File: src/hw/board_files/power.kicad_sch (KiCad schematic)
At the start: 38 parts, among them J1 Conn_01x03_Pin, J6 Screw_Terminal_01x03, P1 USB_C_Plug_USB2.0, SW1 SW_PWR, U1 FT234XD-R, U2 MCP73871, U3 TPS63031DSKR

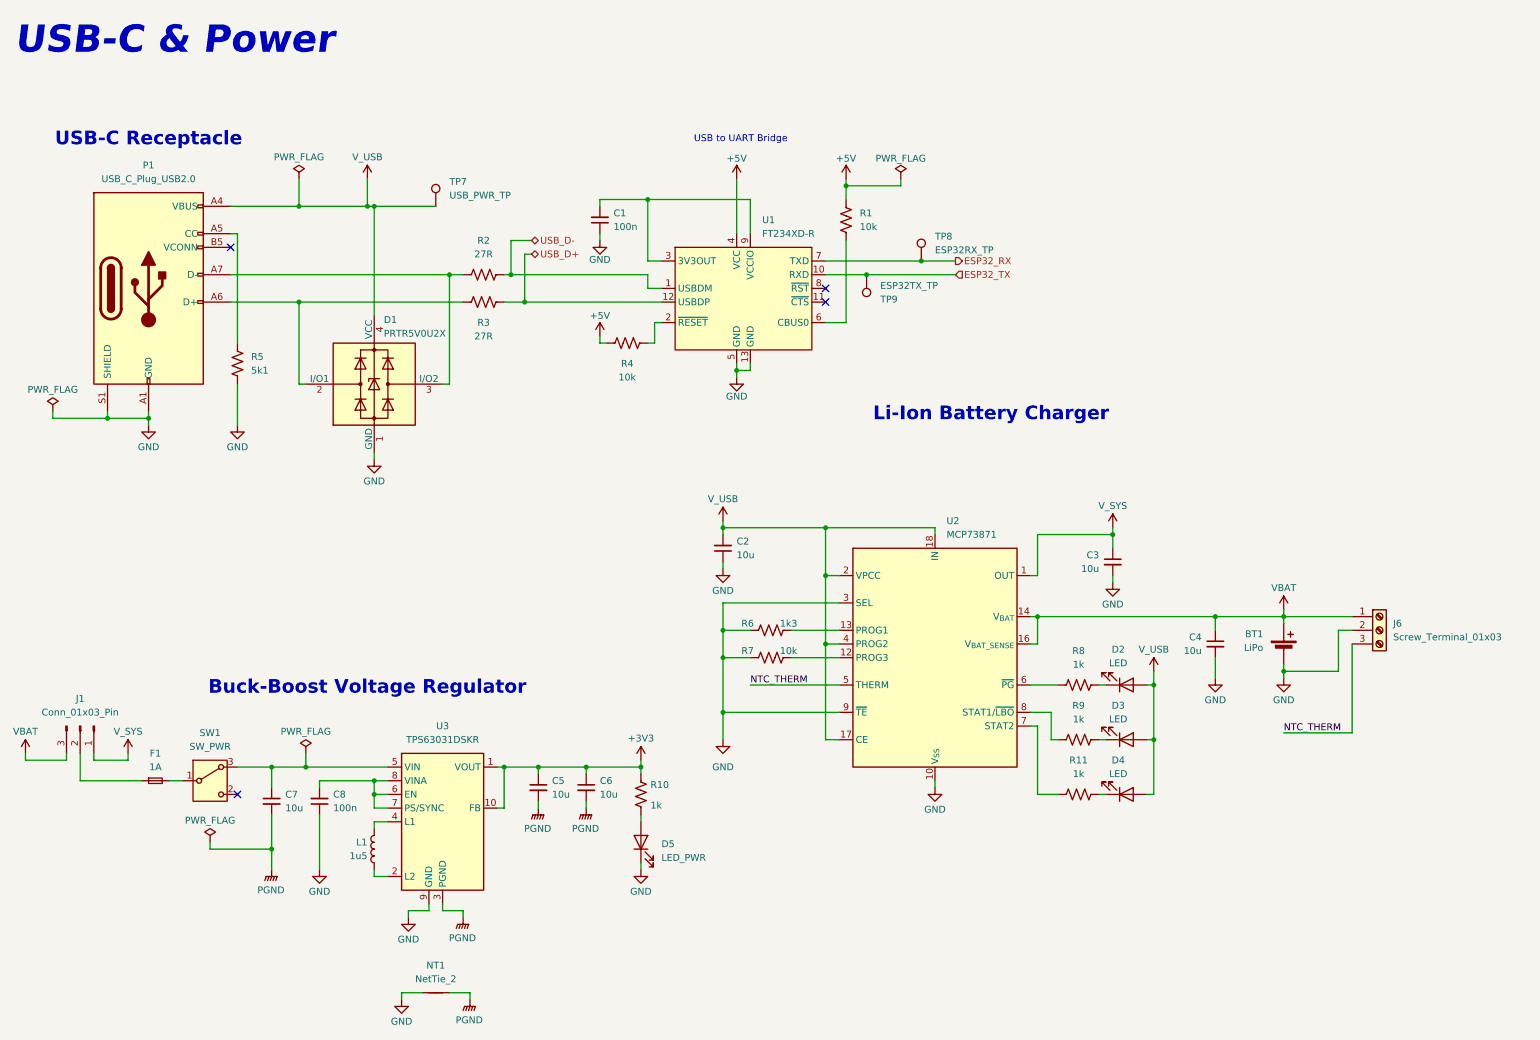
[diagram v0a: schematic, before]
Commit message: Lots of layout progress, changed some references (need to update BOM)
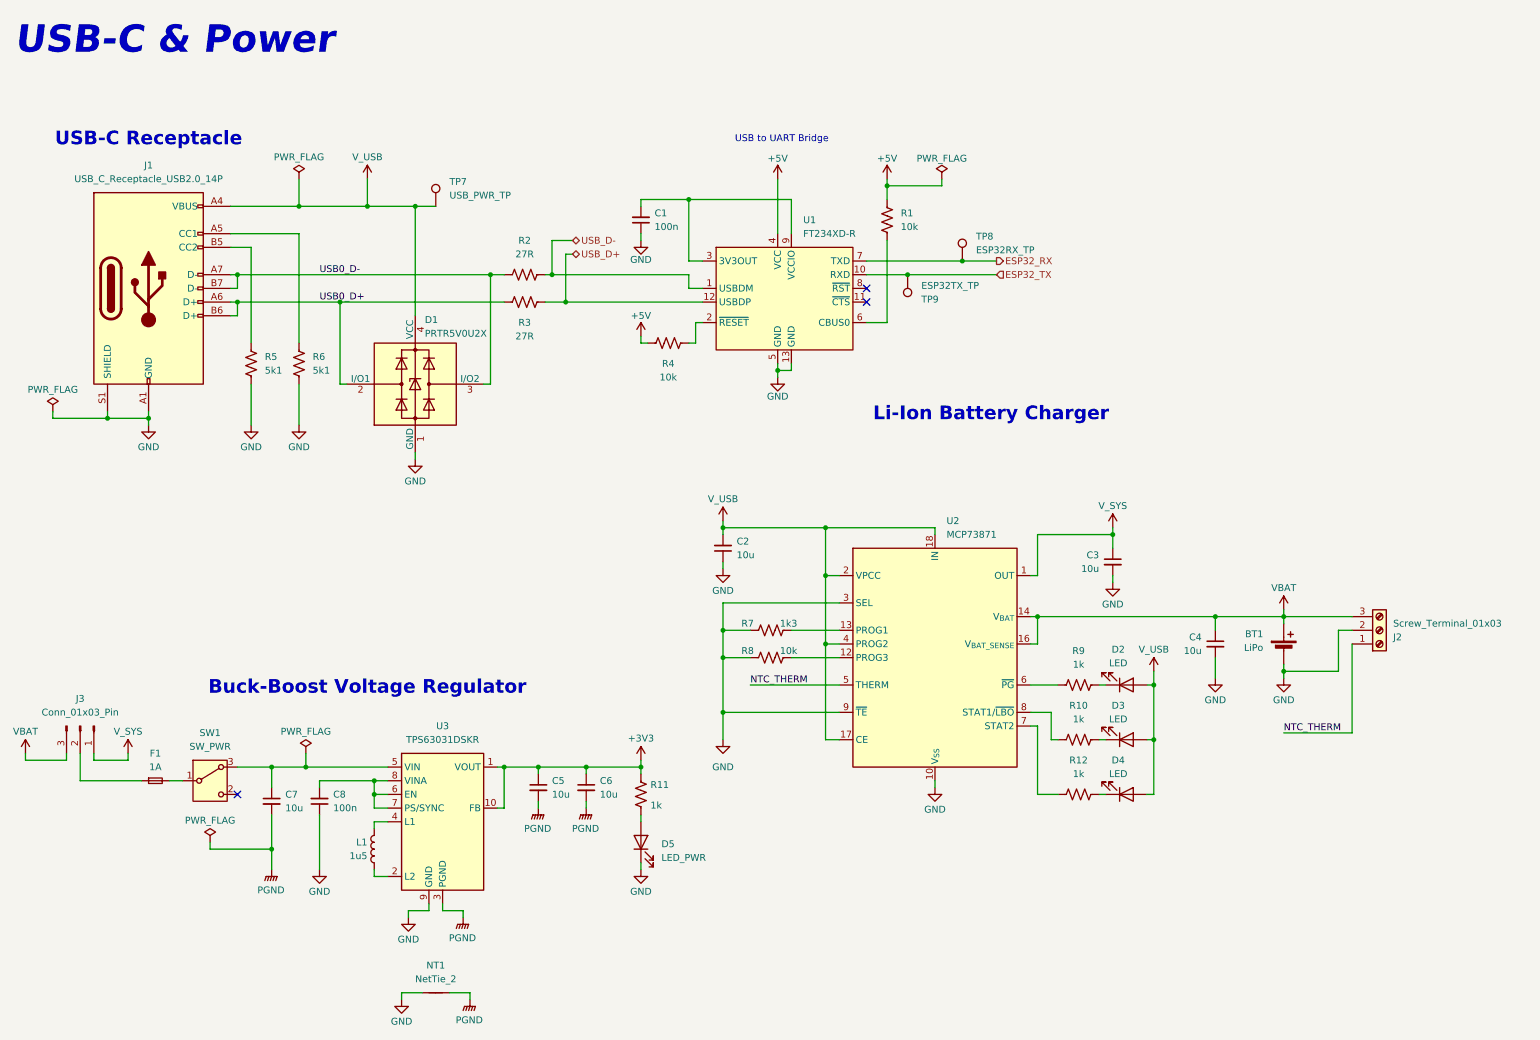
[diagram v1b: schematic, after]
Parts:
- removed P1: USB_C_Plug_USB2.0, Connector_USB:USB_C_Receptacle_GCT_USB4110, symbol Connector:USB_C_Plug_USB2.0
- added J1: USB_C_Receptacle_USB2.0_14P, Connector_USB:USB_C_Receptacle_GCT_USB4105-xx-A_16P_TopMnt_Horizontal, symbol Connector:USB_C_Receptacle_USB2.0_14P
- added R5: 5k1, Resistor_SMD:R_0603_1608Metric_Pad0.98x0.95mm_HandSolder, symbol Device:R_US
- renumbered J6 to J2, J1 to J3, R9 to R10, R10 to R11, R11 to R12, R5 to R6, R6 to R7, R7 to R8, R8 to R9
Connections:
- net GND: now also J1.A1 (GND), J1.A12 (GND), J1.B1 (GND), J1.B12 (GND), J1.S1 (SHIELD), R5.1
- net NTC_THERM: now also J2.1 (Pin_1); no longer J2.3 (Pin_3)
- net VBAT: now also J2.3 (Pin_3); no longer J2.1 (Pin_1)
- net V_USB: now also J1.A4 (VBUS), J1.A9 (VBUS), J1.B4 (VBUS), J1.B9 (VBUS)
- net USB0_D-: now reaches D1.3 (I/O2), R2.2
- net USB0_D-: now also J1.A7 (D-), J1.B7 (D-)
- net USB0_D+: now reaches D1.2 (I/O1), R3.2
- net USB0_D+: now also J1.A6 (D+), J1.B6 (D+)
- net at R6.2: now also J1.A5 (CC1)
- new net: J1.B5 (CC2), R5.2
- no-connect marks 4 -> 3
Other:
- moved on the sheet: C1, D1, R1, R2, R3, R4, R6, TP8, TP9, U1

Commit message: Layout updates
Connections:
- net +5V is gone; now on net +3V3: R1.1, R4.2, U1.4 (VCC)
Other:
- moved on the sheet: BT1, C2, C3, C4, C5, C6, C7, C8, D2, D3, D4, D5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

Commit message: Minor schematic updates
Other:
- note added: "LiPo Battery"
- note added: "LiPo Battery Charger"
- note removed: "Li-Ion Battery Charger"
- moved on the sheet: BT1, J2
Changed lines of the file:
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@@
 	(text "USB-C Receptacle"
 		(exclude_from_sim no)
-		(at 39.37 37.084 0)
+		(at 40.386 34.036 0)
 		(effects
 			(font
@@
 		)
 	)
-	(text "Li-Ion Battery Charger"
+	(text "LiPo Battery Charger"
 		(exclude_from_sim no)
 		(at 204.724 102.362 0)
@@
 	(text "USB to UART Bridge"
 		(exclude_from_sim no)
-		(at 156.972 37.084 0)
+		(at 155.702 34.036 0)
 		(effects
 			(font
-				(size 1.27 1.27)
+				(size 2.54 2.54)
+				(thickness 0.508)
+				(bold yes)
+			)
+		)
+	)
+	(text "LiPo Battery"
+		(exclude_from_sim no)
+		(at 240.284 34.544 0)
+		(effects
+			(font
+				(size 2.54 2.54)
+				(thickness 0.508)
+				(bold yes)
 			)
 		)
@@
 	)
 	(junction
-		(at 219.71 35.56)
+		(at 224.79 62.23)
 		(diameter 0)
 		(color 0 0 0 0)
@@
 	)
 	(junction
-		(at 219.71 25.4)
+		(at 224.79 52.07)
 		(diameter 0)
 		(color 0 0 0 0)
@@
 	(wire
 		(pts
-			(xy 219.71 34.29) (xy 219.71 35.56)
+			(xy 224.79 60.96) (xy 224.79 62.23)
 		)
 		(stroke
@@
 	(wire
 		(pts
-			(xy 219.71 25.4) (xy 219.71 26.67)
+			(xy 224.79 52.07) (xy 224.79 53.34)
 		)
 		(stroke
@@
 	(wire
 		(pts
-			(xy 232.41 30.48) (xy 232.41 46.99)
+			(xy 237.49 57.15) (xy 237.49 73.66)
 		)
 		(stroke
@@
 	(wire
 		(pts
-			(xy 232.41 27.94) (xy 229.87 27.94)
+			(xy 237.49 54.61) (xy 234.95 54.61)
 		)
 		(stroke
@@
 	(wire
 		(pts
-			(xy 219.71 46.99) (xy 232.41 46.99)
+			(xy 224.79 73.66) (xy 237.49 73.66)
 		)
 		(stroke
@@
 	(wire
 		(pts
-			(xy 219.71 35.56) (xy 219.71 36.83)
+			(xy 224.79 62.23) (xy 224.79 63.5)
 		)
 		(stroke
@@
 	(wire
 		(pts
-			(xy 229.87 27.94) (xy 229.87 35.56)
+			(xy 234.95 54.61) (xy 234.95 62.23)
 		)
 		(stroke
@@
 	(wire
 		(pts
-			(xy 219.71 24.13) (xy 219.71 25.4)
+			(xy 224.79 50.8) (xy 224.79 52.07)
 		)
 		(stroke
@@
 	(wire
 		(pts
-			(xy 229.87 35.56) (xy 219.71 35.56)
+			(xy 234.95 62.23) (xy 224.79 62.23)
 		)
 		(stroke
@@
 	(wire
 		(pts
-			(xy 219.71 25.4) (xy 232.41 25.4)
+			(xy 224.79 52.07) (xy 237.49 52.07)
 		)
 		(stroke
@@
 	)
 	(label "NTC_THERM"
-		(at 219.71 46.99 0)
+		(at 224.79 73.66 0)
 		(effects
 			(font
@@
 	(symbol
 		(lib_id "power:GND")
-		(at 219.71 36.83 0)
+		(at 224.79 63.5 0)
 		(unit 1)
 		(exclude_from_sim no)
@@
 		(dnp no)
 		(property "Reference" "#PWR018"
-			(at 219.71 43.18 0)
+			(at 224.79 69.85 0)
 			(effects
 				(font
@@
 		)
 		(property "Value" "GND"
-			(at 219.71 40.894 0)
+			(at 224.79 67.564 0)
 			(effects
 				(font
@@
 		)
 		(property "Footprint" ""
-			(at 219.71 36.83 0)
+			(at 224.79 63.5 0)
 			(effects
 				(font
@@
 		)
 		(property "Datasheet" ""
-			(at 219.71 36.83 0)
+			(at 224.79 63.5 0)
 			(effects
 				(font
@@
 		)
 		(property "Description" "Power symbol creates a global label with name \"GND\" , ground"
-			(at 219.71 36.83 0)
+			(at 224.79 63.5 0)
 			(effects
 				(font
@@
 	(symbol
 		(lib_id "Connector:Screw_Terminal_01x03")
-		(at 237.49 27.94 0)
+		(at 242.57 54.61 0)
 		(mirror x)
 		(unit 1)
@@
 		(dnp no)
 		(property "Reference" "J2"
-			(at 240.03 29.2101 0)
+			(at 245.11 55.8801 0)
 			(effects
 				(font
@@
 		)
 		(property "Value" "Screw_Terminal_01x03"
-			(at 240.03 26.6701 0)
+			(at 245.11 53.3401 0)
 			(effects
 				(font
@@
 		)
 		(property "Footprint" "TerminalBlock_Phoenix:TerminalBlock_Phoenix_MPT-0,5-3-2.54_1x03_P2.54mm_Horizontal"
-			(at 237.49 27.94 0)
+			(at 242.57 54.61 0)
 			(effects
 				(font
@@
 		)
 		(property "Datasheet" "~"
-			(at 237.49 27.94 0)
+			(at 242.57 54.61 0)
 			(effects
 				(font
@@
 		)
 		(property "Description" "Generic screw terminal, single row, 01x03, script generated (kicad-library-utils/schlib/autogen/connector/)"
-			(at 237.49 27.94 0)
+			(at 242.57 54.61 0)
 			(effects
 				(font
@@
 	(symbol
 		(lib_id "power:+3V3")
-		(at 219.71 24.13 0)
+		(at 224.79 50.8 0)
 		(unit 1)
 		(exclude_from_sim no)
@@
 		(dnp no)
 		(property "Reference" "#PWR081"
-			(at 219.71 27.94 0)
+			(at 224.79 54.61 0)
 			(effects
 				(font
@@
 		)
 		(property "Value" "VBAT"
-			(at 219.71 20.066 0)
+			(at 224.79 46.736 0)
 			(effects
 				(font
@@
 		)
 		(property "Footprint" ""
-			(at 219.71 24.13 0)
+			(at 224.79 50.8 0)
 			(effects
 				(font
@@
 		)
 		(property "Datasheet" ""
-			(at 219.71 24.13 0)
+			(at 224.79 50.8 0)
 			(effects
 				(font
@@
 		)
 		(property "Description" "Power symbol creates a global label with name \"+3V3\""
-			(at 219.71 24.13 0)
+			(at 224.79 50.8 0)
 			(effects
 				(font
@@
 	(symbol
 		(lib_id "Device:Battery_Cell")
-		(at 219.71 31.75 0)
+		(at 224.79 58.42 0)
 		(unit 1)
 		(exclude_from_sim no)
@@
 		(fields_autoplaced yes)
 		(property "Reference" "BT1"
-			(at 215.9 28.6384 0)
+			(at 220.98 55.3084 0)
 			(effects
 				(font
@@
 		)
 		(property "Value" "LiPo"
-			(at 215.9 31.1784 0)
+			(at 220.98 57.8484 0)
 			(effects
 				(font
@@
 		)
 		(property "Footprint" "Connector_JST:JST_PH_S2B-PH-K_1x02_P2.00mm_Horizontal"
-			(at 219.71 30.226 90)
+			(at 224.79 56.896 90)
 			(effects
 				(font
@@
 		)
 		(property "Datasheet" "https://www.adafruit.com/product/328"
-			(at 219.71 30.226 90)
+			(at 224.79 56.896 90)
 			(effects
 				(font
@@
 		)
 		(property "Description" "Single-cell battery"
-			(at 219.71 31.75 0)
+			(at 224.79 58.42 0)
 			(effects
 				(font

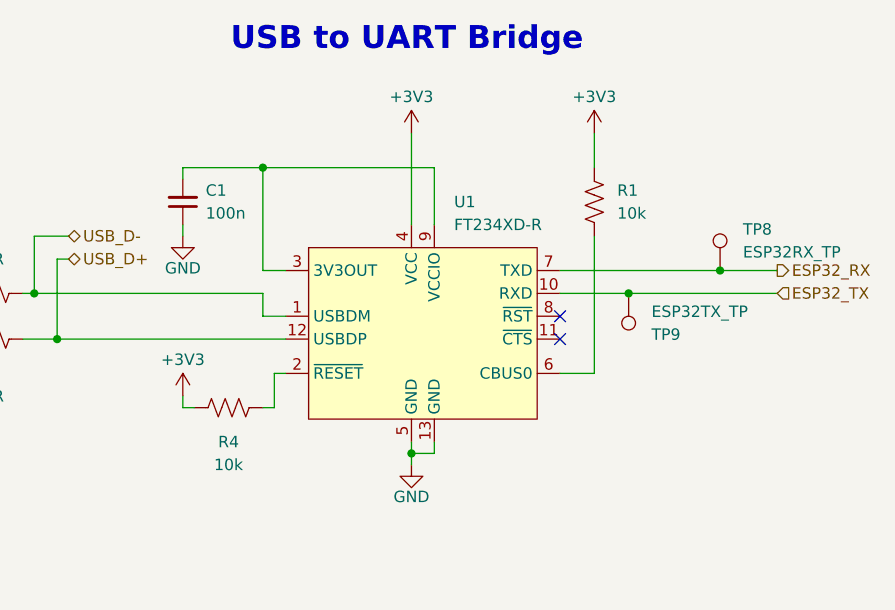
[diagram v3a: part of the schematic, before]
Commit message: Changed fuel gauge IC. Need to update component references and BOM.
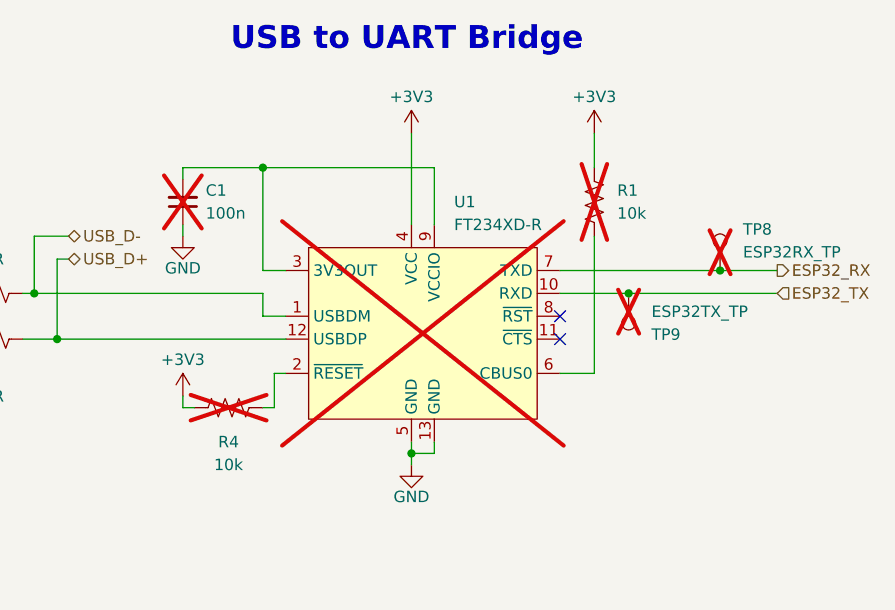
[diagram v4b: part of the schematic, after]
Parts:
- C1, R1, R4, TP8, TP9, U1: now not fitted
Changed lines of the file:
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@@
 		(exclude_from_sim no)
 		(in_bom yes)
-		(on_board yes)
-		(dnp no)
+		(on_board no)
+		(dnp yes)
 		(fields_autoplaced yes)
 		(property "Reference" "U1"
@@
 		(exclude_from_sim no)
 		(in_bom yes)
-		(on_board yes)
-		(dnp no)
+		(on_board no)
+		(dnp yes)
 		(fields_autoplaced yes)
 		(property "Reference" "R1"
@@
 		(exclude_from_sim no)
 		(in_bom yes)
-		(on_board yes)
-		(dnp no)
+		(on_board no)
+		(dnp yes)
 		(fields_autoplaced yes)
 		(property "Reference" "C1"
@@
 		(exclude_from_sim no)
 		(in_bom yes)
-		(on_board yes)
-		(dnp no)
+		(on_board no)
+		(dnp yes)
 		(property "Reference" "TP9"
 			(at 182.88 66.8021 0)
@@
 		(exclude_from_sim no)
 		(in_bom yes)
-		(on_board yes)
-		(dnp no)
+		(on_board no)
+		(dnp yes)
 		(fields_autoplaced yes)
 		(property "Reference" "R4"
@@
 		(exclude_from_sim no)
 		(in_bom yes)
-		(on_board yes)
-		(dnp no)
+		(on_board no)
+		(dnp yes)
 		(fields_autoplaced yes)
 		(property "Reference" "TP8"

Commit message: Layout progress. Made new footprint for inductor. Changed test  points to pads
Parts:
- L1: footprint Inductor_SMD:L_Coilcraft_LPS3010 -> Project_Library:TDK_VLS3012_3.0x3.0mm
- TP7: footprint TestPoint:TestPoint_Loop_D2.54mm_Drill1.5mm_Beaded -> TestPoint:TestPoint_Pad_D1.5mm; now left out of the parts list
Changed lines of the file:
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@@
 		(unit 1)
 		(exclude_from_sim no)
-		(in_bom yes)
+		(in_bom no)
 		(on_board yes)
 		(dnp no)
@@
 			)
 		)
-		(property "Footprint" "TestPoint:TestPoint_Loop_D2.54mm_Drill1.5mm_Beaded"
+		(property "Footprint" "TestPoint:TestPoint_Pad_D1.5mm"
 			(at 97.79 49.53 0)
 			(effects
@@
 			)
 		)
-		(property "Footprint" "Inductor_SMD:L_Coilcraft_LPS3010"
+		(property "Footprint" "Project_Library:TDK_VLS3012_3.0x3.0mm"
 			(at 81.28 167.64 0)
 			(effects

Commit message: Updated BOM
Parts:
- removed C1: 100n, Capacitor_SMD:C_0603_1608Metric_Pad1.08x0.95mm_HandSolder, symbol Device:C_Small
- removed R1, R4: 10k, Resistor_SMD:R_0603_1608Metric_Pad0.98x0.95mm_HandSolder, symbol Device:R_US
- removed TP8: ESP32RX_TP, TestPoint:TestPoint_Loop_D2.54mm_Drill1.5mm_Beaded, symbol Connector:TestPoint
- removed TP9: ESP32TX_TP, TestPoint:TestPoint_Loop_D2.54mm_Drill1.5mm_Beaded, symbol Connector:TestPoint
- removed U1: FT234XD-R, Package_DFN_QFN:DFN-12-1EP_3x3mm_P0.45mm_EP1.65x2.38mm, symbol smart_clock:FT234XD-R
- renumbered C2 to C1, C3 to C2, C4 to C3, C5 to C4, C6 to C5, C7 to C6, C8 to C7, D2 to D1, D1 to D2, R2 to R1, R11 to R10, R7 to R2, R8 to R4, R9 to R5, R5 to R6, R6 to R7, R10 to R8, R12 to R9, U2 to U1, U3 to U2
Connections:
- no-connect marks 3 -> 1
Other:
- note removed: "USB to UART Bridge"
- moved on the sheet: BT1, C1, C2, C3, D1, D3, D4, J2, R2, R4, R5, R8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
